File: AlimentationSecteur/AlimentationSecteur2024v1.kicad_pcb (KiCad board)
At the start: 2 copper layers, 75 x 49 mm, 15 parts

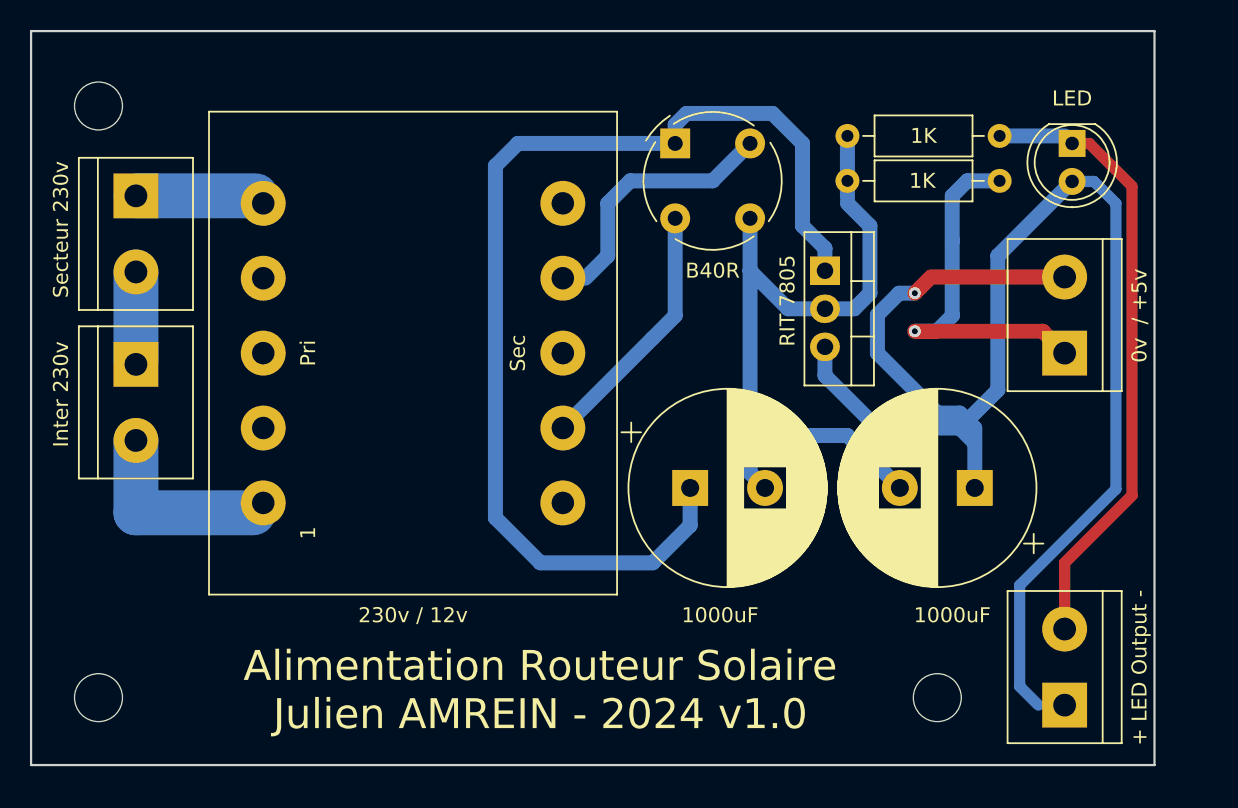
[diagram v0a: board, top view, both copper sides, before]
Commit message: MAJ Alimentation - ajout du bornier 5 volts alternatif et MAJ du GERBER Alimentation
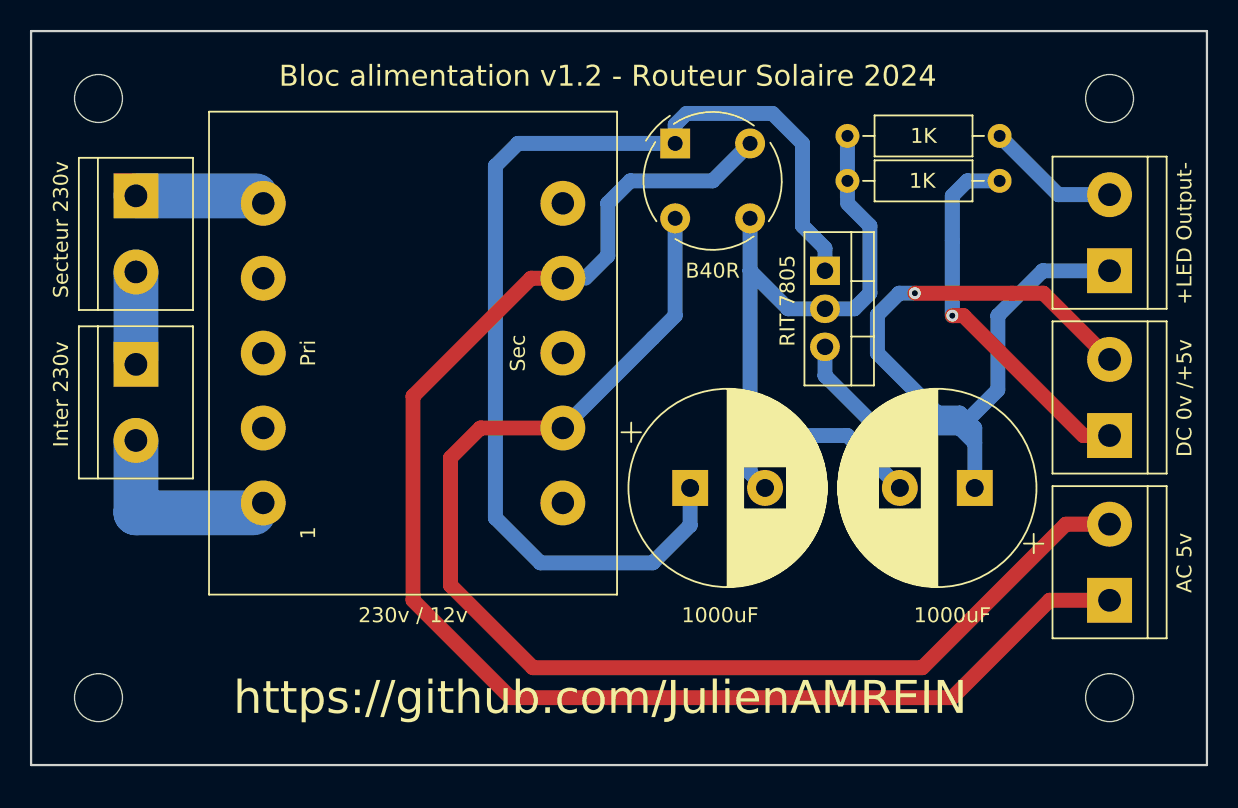
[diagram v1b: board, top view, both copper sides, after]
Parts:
- removed LED: LED_D5.0mm, LED_THT:LED_D5.0mm
- added ?: MountingHole_3.2mm_M3, MountingHole:MountingHole_3.2mm_M3, F.Cu at (180.5, 80.5)
- added AC 5v: TerminalBlock_bornier-2_P5.08mm, TerminalBlock:TerminalBlock_bornier-2_P5.08mm, F.Cu at (180.5, 114.0)
- +LED Output-: renamed from + LED Output -
- DC 0v /+5v: renamed from 0v  / +5v
- moved +LED Output- 29.2 mm to (180.5, 92.0)
- moved ? 11.5 mm to (180.5, 120.5)
- moved DC 0v /+5v 6.26 mm to (180.5, 103.0)
- moved ? 0.50 mm to (113.0, 80.5)
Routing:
- net (no net): track 362.8 -> 436.3 mm
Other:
- board size 75 x 49 mm -> 78.5 x 49 mm
- board text added: "Bloc alimentation v1.2 - Routeur Solaire 2024"
- board text added: "https://github.com/JulienAMREIN"
- board text removed: "Alimentation Routeur Solaire Julien AMREIN - 2024 v1.0"

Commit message: Ajout de la carte basse tension au dépot
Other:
- board text added: "Carte alimentation v1.2 - Routeur Solaire 2024"
- board text removed: "Bloc alimentation v1.2 - Routeur Solaire 2024"
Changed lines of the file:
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@@
     (pad 1 np_thru_hole circle (at 0 0) (size 3.2 3.2) (drill 3.2) (layers *.Cu *.Mask))
   )
-  (gr_text "Bloc alimentation v1.2 - Routeur Solaire 2024" (at 147 79) (layer F.SilkS)
+  (gr_text "Carte alimentation v1.2 - Routeur Solaire 2024" (at 147 79) (layer F.SilkS)
     (effects (font (size 1.4 1.4) (thickness 0.25)))
   )
